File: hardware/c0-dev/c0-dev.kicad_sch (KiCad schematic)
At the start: 1 part, among them J3 Conn_01x05

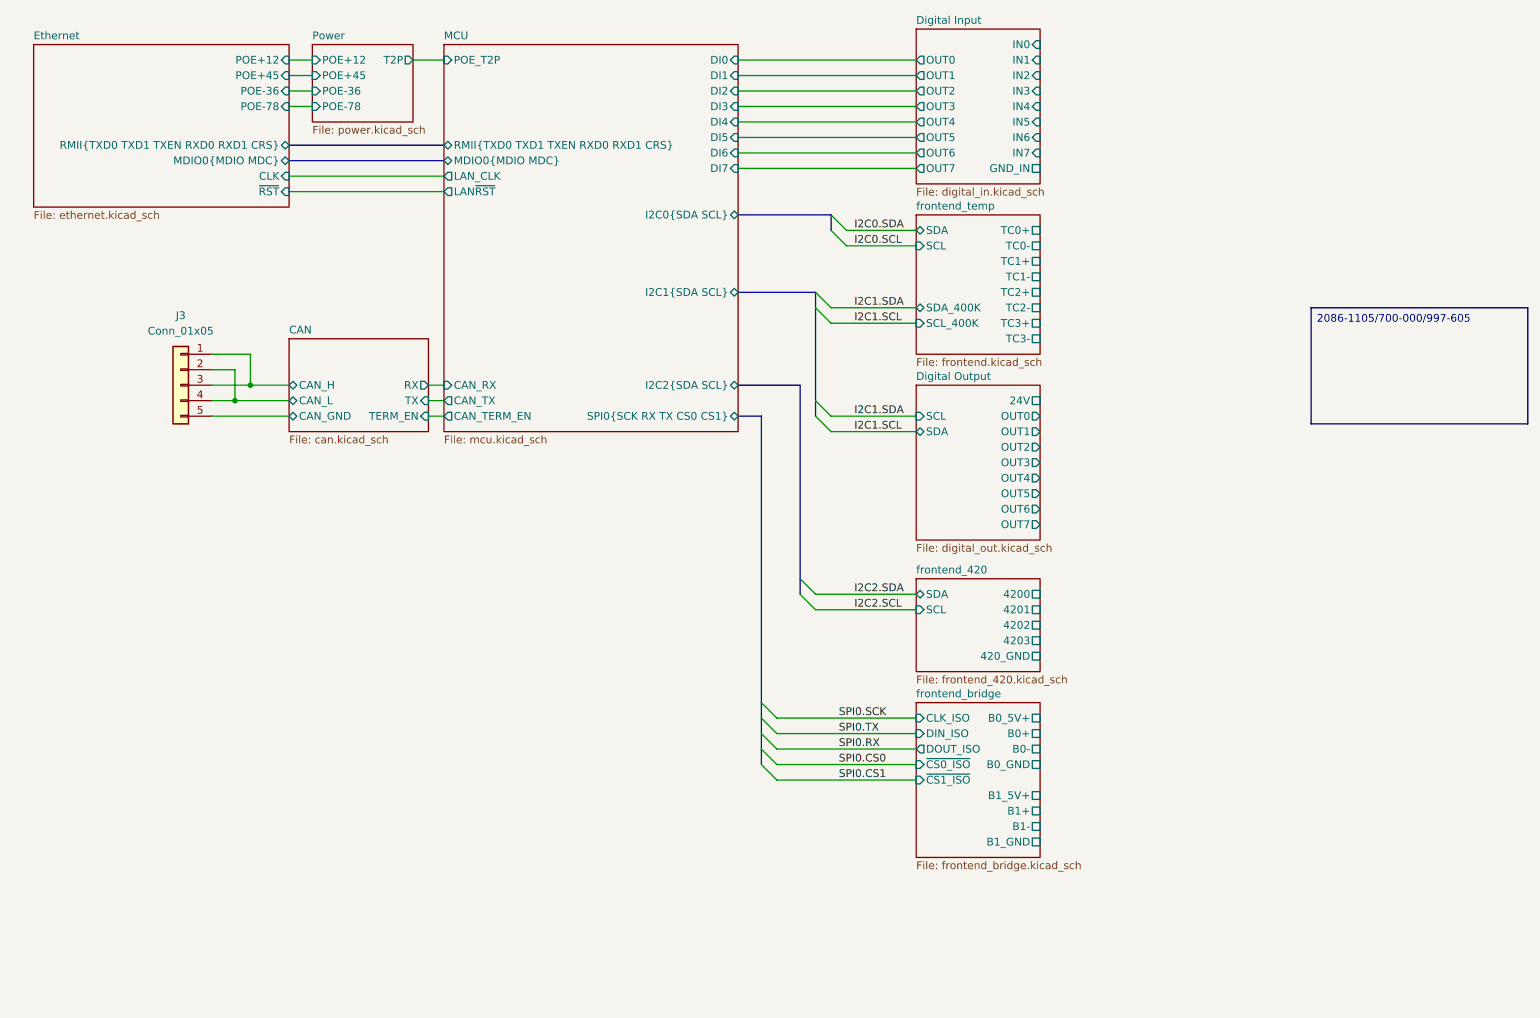
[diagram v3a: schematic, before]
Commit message: added connectors
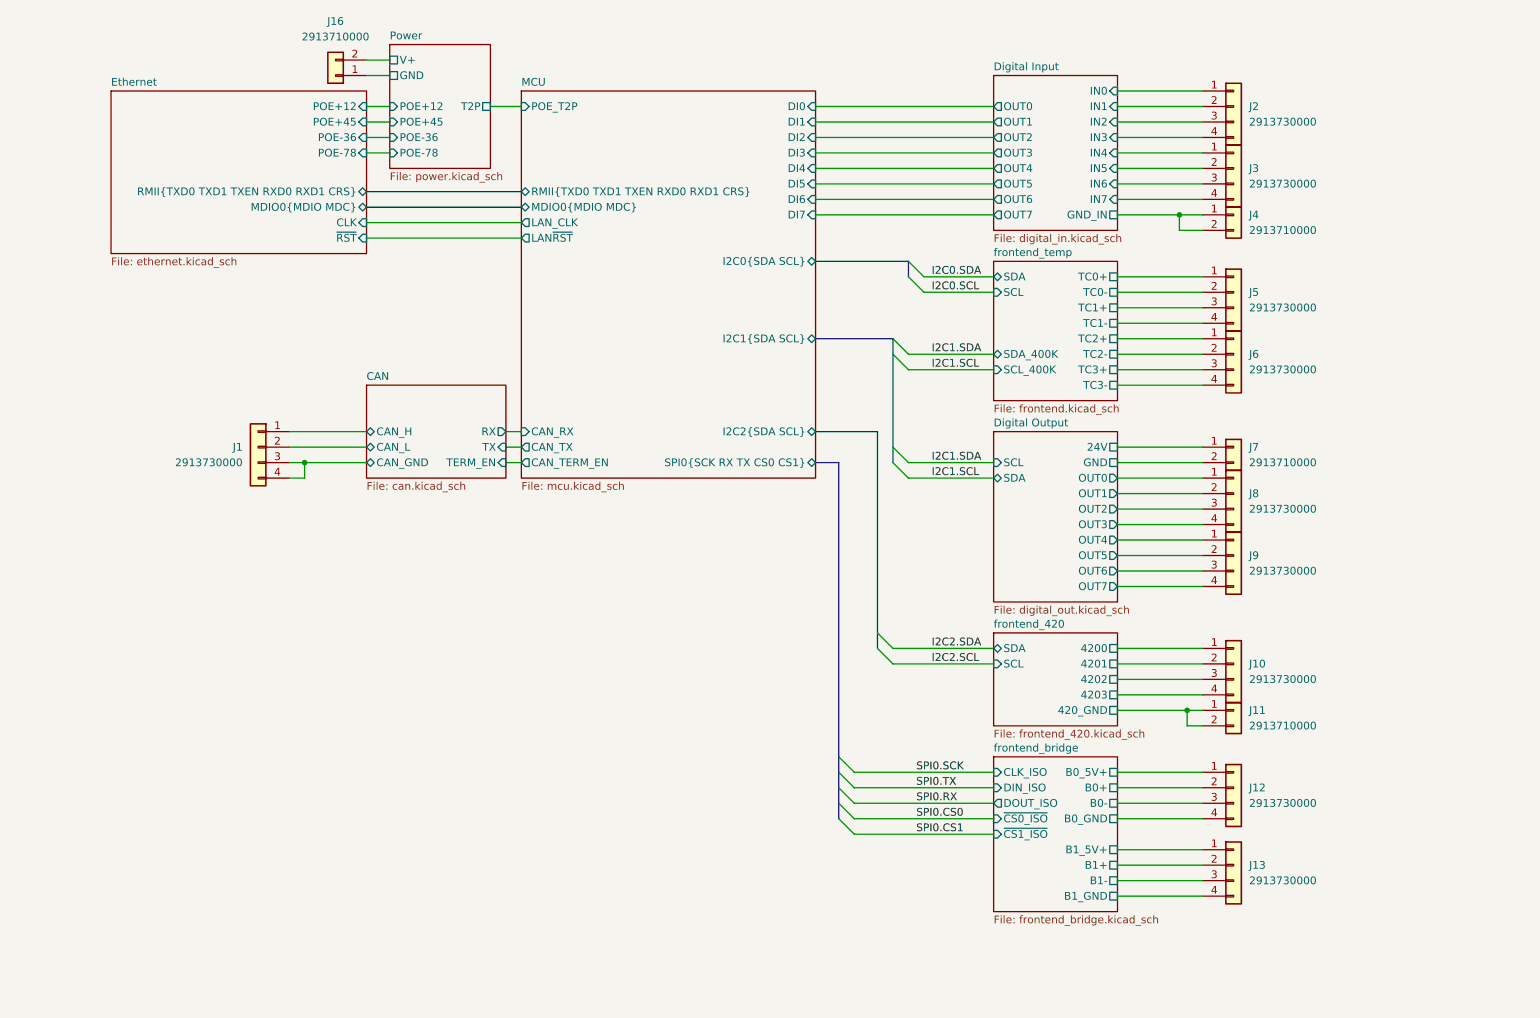
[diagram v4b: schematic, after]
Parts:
- removed J3: Conn_01x05, symbol Connector_Generic:Conn_01x05
- added J1, J10, J12, J13, J2, J3, J5, J6, J8, J9: 2913730000, symbol Connector_Generic:Conn_01x04
- added J11, J16, J4, J7: 2913710000, symbol Connector_Generic:Conn_01x02
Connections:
- net CAN/CAN_GND: now also J1.3 (Pin_3), J1.4 (Pin_4)
- net CAN/CAN_H: now also J1.1 (Pin_1)
- net CAN/CAN_L: now also J1.2 (Pin_2)
- net Digital Input/GND_IN: now also J4.1 (Pin_1), J4.2 (Pin_2)
- net Digital Input/IN0: now also J2.1 (Pin_1)
- net Digital Input/IN1: now also J2.2 (Pin_2)
- net Digital Input/IN2: now also J2.3 (Pin_3)
- net Digital Input/IN3: now also J2.4 (Pin_4)
- net Digital Input/IN4: now also J3.1 (Pin_1)
- net Digital Input/IN5: now also J3.2 (Pin_2)
- net Digital Input/IN6: now also J3.3 (Pin_3)
- net Digital Input/IN7: now also J3.4 (Pin_4)
- net Digital Output/24V: now also J7.1 (Pin_1)
- net Digital Output/OUT0: now also J8.1 (Pin_1)
- net Digital Output/OUT1: now also J8.2 (Pin_2)
- net Digital Output/OUT2: now also J8.3 (Pin_3)
- net Digital Output/OUT3: now also J8.4 (Pin_4)
- net Digital Output/OUT4: now also J9.1 (Pin_1)
- net Digital Output/OUT5: now also J9.2 (Pin_2)
- net Digital Output/OUT6: now also J9.3 (Pin_3)
- net Digital Output/OUT7: now also J9.4 (Pin_4)
- net frontend_420/4200: now also J10.1 (Pin_1)
- net frontend_420/4201: now also J10.2 (Pin_2)
- net frontend_420/4202: now also J10.3 (Pin_3)
- net frontend_420/4203: now also J10.4 (Pin_4)
- net frontend_420/420_GND: now also J11.1 (Pin_1), J11.2 (Pin_2)
- net frontend_bridge/B0+: now also J12.2 (Pin_2)
- net frontend_bridge/B0-: now also J12.3 (Pin_3)
- net frontend_bridge/B0_5V+: now also J12.1 (Pin_1)
- net frontend_bridge/B0_GND: now also J12.4 (Pin_4)
- net frontend_bridge/B1+: now also J13.2 (Pin_2)
- net frontend_bridge/B1-: now also J13.3 (Pin_3)
- net frontend_bridge/B1_5V+: now also J13.1 (Pin_1)
- net frontend_bridge/B1_GND: now also J13.4 (Pin_4)
- net frontend_temp/TC0+: now also J5.1 (Pin_1)
- net frontend_temp/TC0-: now also J5.2 (Pin_2)
- net frontend_temp/TC1+: now also J5.3 (Pin_3)
- net frontend_temp/TC1-: now also J5.4 (Pin_4)
- net frontend_temp/TC2+: now also J6.1 (Pin_1)
- net frontend_temp/TC2-: now also J6.2 (Pin_2)
- net frontend_temp/TC3+: now also J6.3 (Pin_3)
- net frontend_temp/TC3-: now also J6.4 (Pin_4)
- new net Digital Output/GND: J7.2 (Pin_2)
- new net Power/GND: J16.1 (Pin_1)
- new net Power/V+: J16.2 (Pin_2)
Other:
- sheet Digital Output ports: added GND; removed none
- sheet Power ports: added GND, V+; removed none

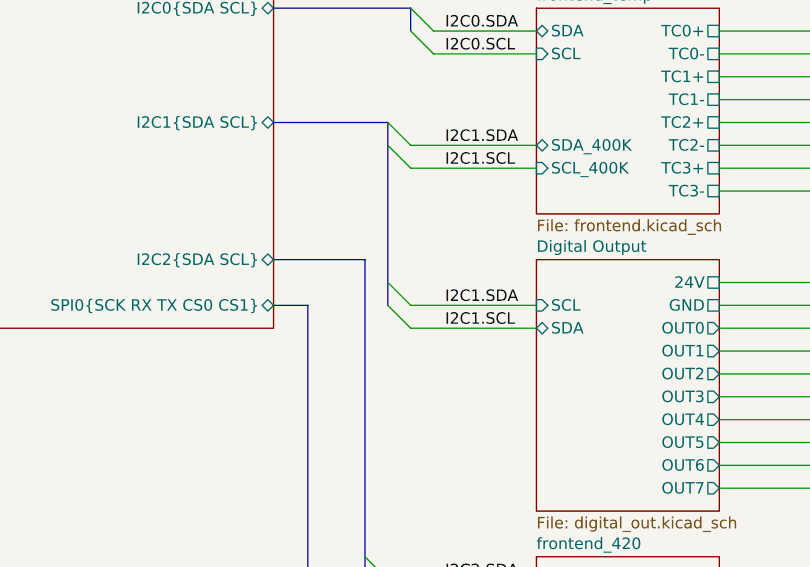
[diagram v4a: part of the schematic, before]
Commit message: added watchdog output disable
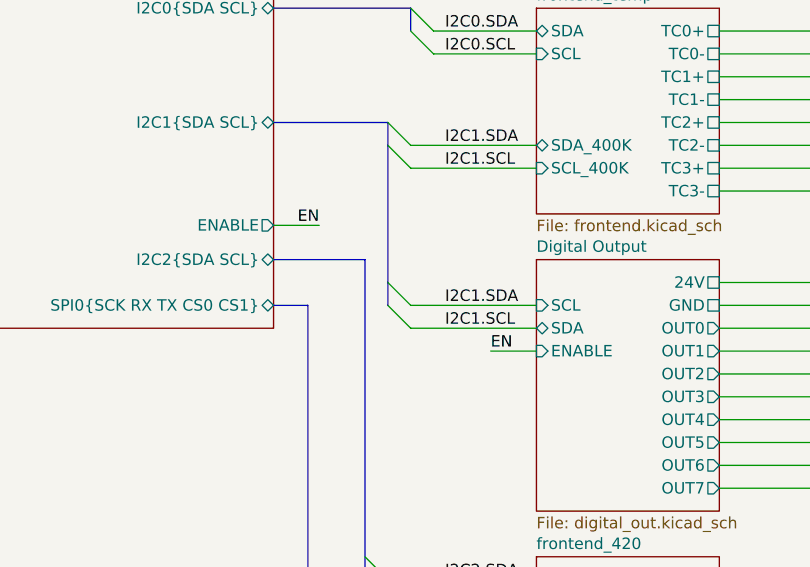
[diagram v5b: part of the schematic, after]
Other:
- sheet Digital Output ports: added ENABLE; removed none
- sheet MCU ports: added ENABLE; removed none
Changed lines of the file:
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@@
+	(wire
+		(pts
+			(xy 148.59 80.01) (xy 153.67 80.01)
+		)
+		(stroke
+			(width 0)
+			(type default)
+		)
+	)
 	(wire
 		(pts
@@
 		(pts
 			(xy 163.83 73.66) (xy 177.8 73.66)
+		)
+		(stroke
+			(width 0)
+			(type default)
+		)
+	)
+	(wire
+		(pts
+			(xy 172.72 93.98) (xy 177.8 93.98)
 		)
 		(stroke
@@
 		)
 	)
+	(label "EN"
+		(at 172.72 93.98 0)
+		(effects
+			(font
+				(size 1.27 1.27)
+			)
+			(justify left bottom)
+		)
+	)
 	(label "I2C0.SCL"
 		(at 167.64 60.96 0)
@@
 			)
 			(justify left bottom)
+		)
+	)
+	(label "EN"
+		(at 153.67 80.01 180)
+		(effects
+			(font
+				(size 1.27 1.27)
+			)
+			(justify right bottom)
 		)
 	)
@@
 			)
 		)
+		(pin "ENABLE" input
+			(at 177.8 93.98 180)
+			(effects
+				(font
+					(size 1.27 1.27)
+				)
+				(justify left)
+			)
+		)
 		(instances
 			(project "c0-dev"
@@
 			(effects
 				(font
+					(size 1.27 1.27)
+				)
+				(justify right)
+			)
+		)
+		(pin "ENABLE" output
+			(at 148.59 80.01 0)
+			(effects
+				(font

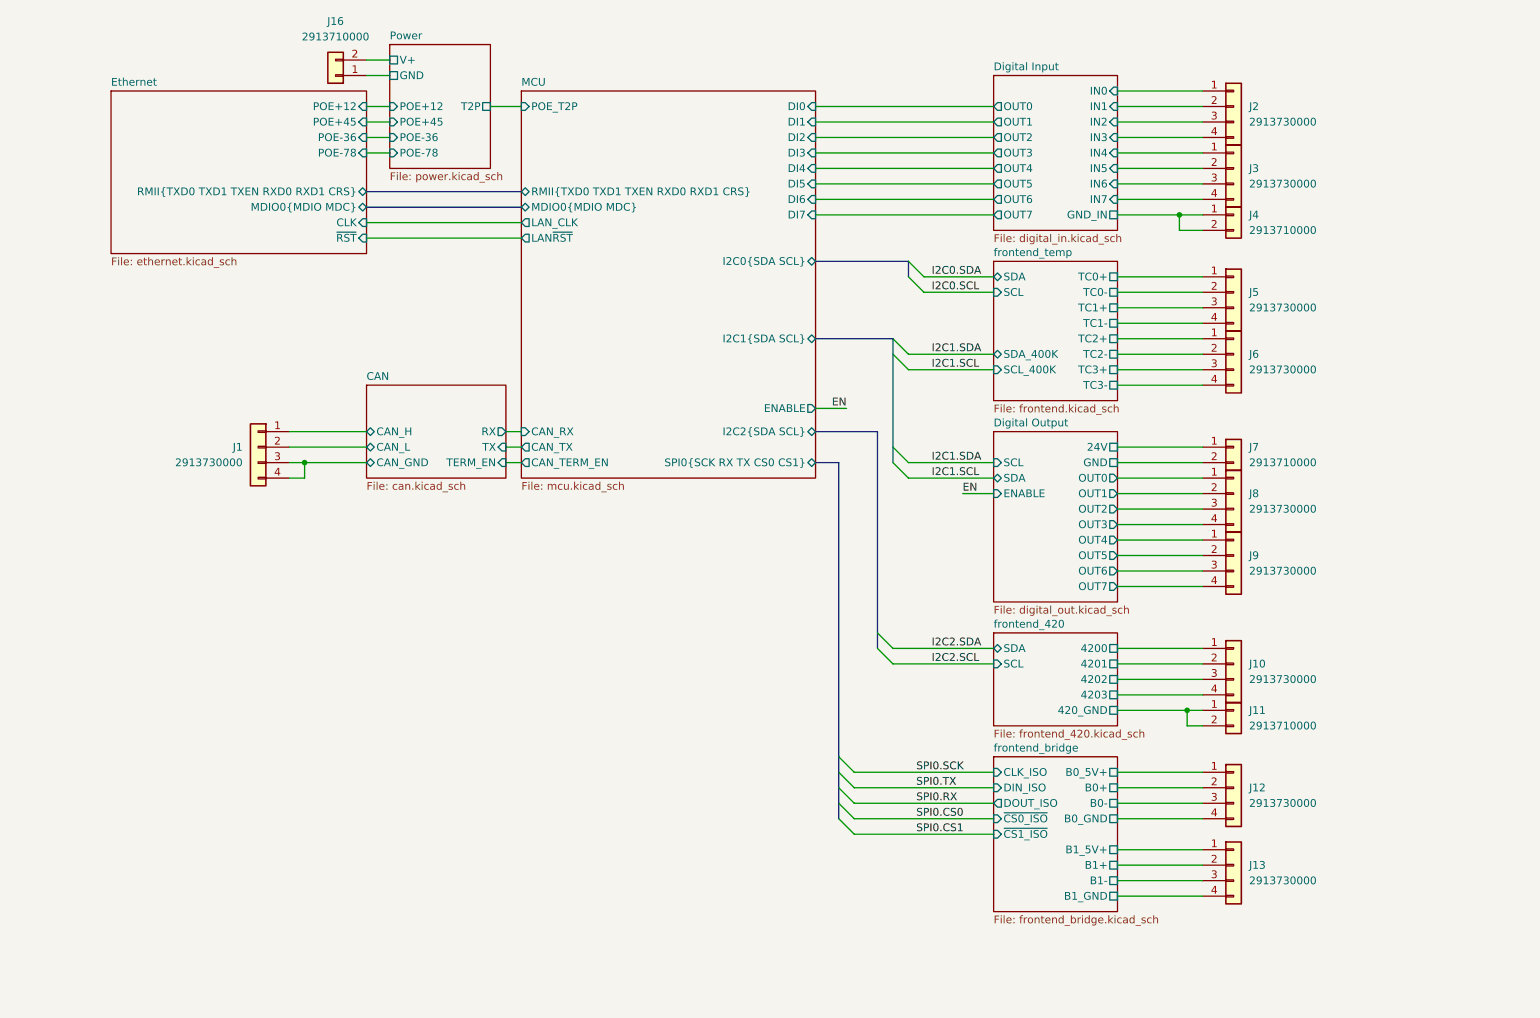
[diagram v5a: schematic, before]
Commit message: added 4-pin connector
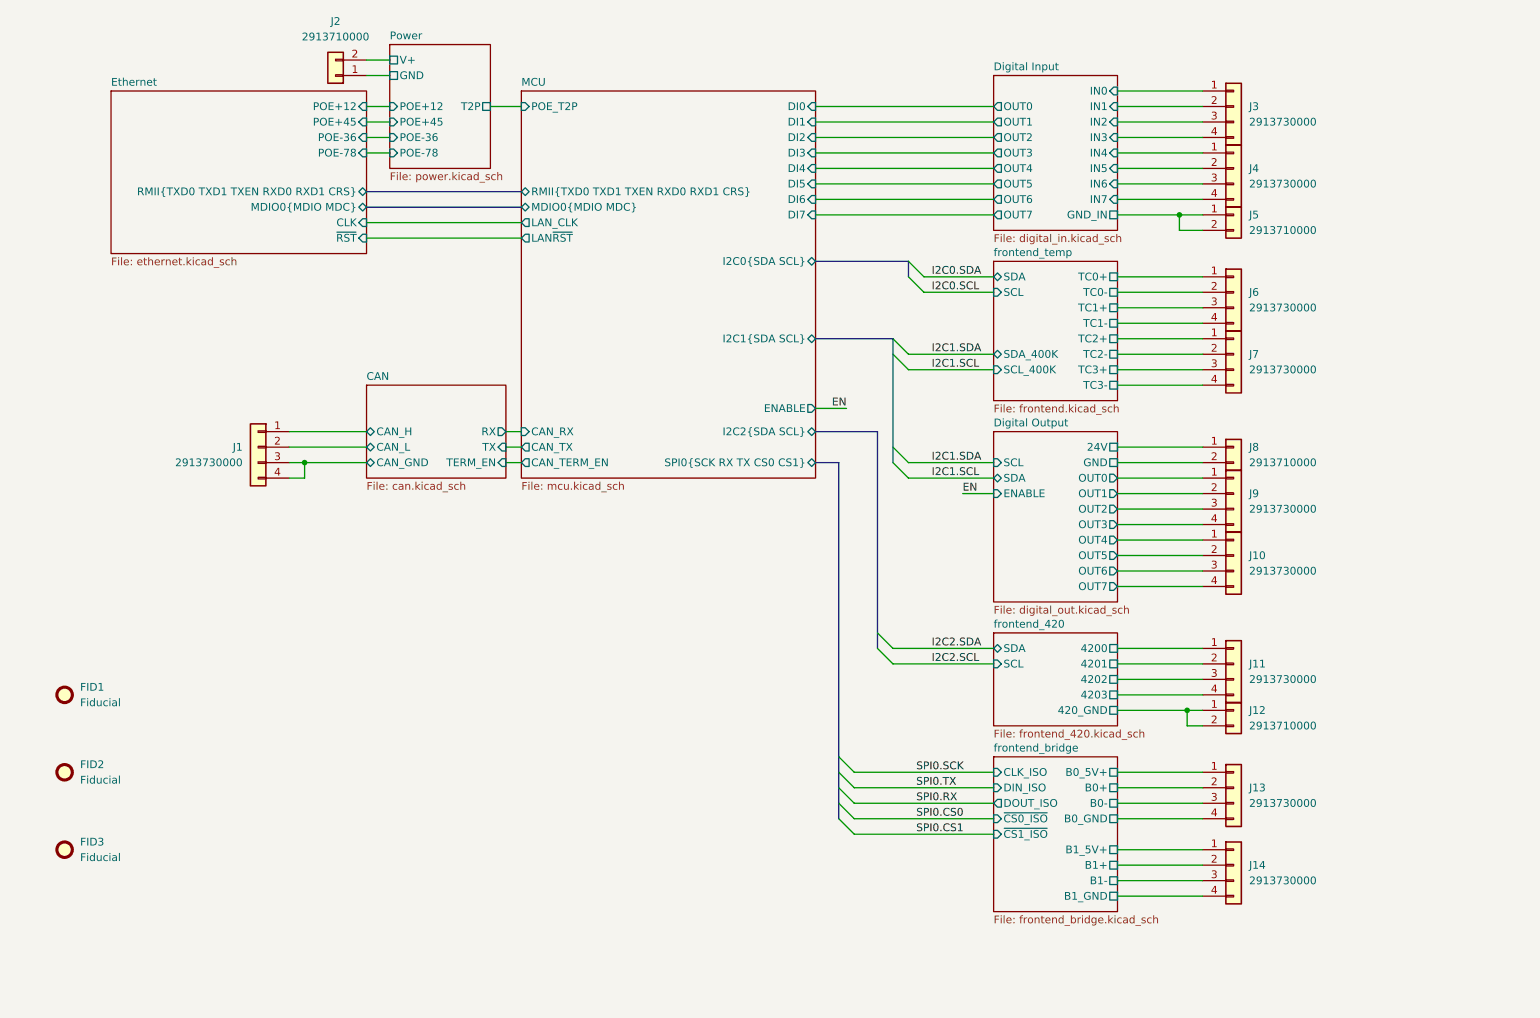
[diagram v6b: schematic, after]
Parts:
- removed J12, J3, J5, J8: 2913730000, symbol Connector_Generic:Conn_01x04
- added FID1, FID2, FID3: Fiducial, Fiducial:Fiducial_1mm_Mask2mm, symbol Mechanical:Fiducial
- added J11, J14, J4, J7: 2913730000, conduit:2913730000, symbol Connector_Generic:Conn_01x04
- J1, J10, J13, J6, J9: footprint (none) -> conduit:2913730000
- J3: renamed from J2; footprint (none) -> conduit:2913730000
- renumbered J11 to J12, J16 to J2, J4 to J5, J7 to J8
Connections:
- net Digital Input/IN4: now also J4.1 (Pin_1)
- net Digital Input/IN5: now also J4.2 (Pin_2)
- net Digital Input/IN6: now also J4.3 (Pin_3)
- net Digital Input/IN7: now also J4.4 (Pin_4)
- net Digital Output/OUT0: now also J9.1 (Pin_1)
- net Digital Output/OUT1: now also J9.2 (Pin_2)
- net Digital Output/OUT2: now also J9.3 (Pin_3)
- net Digital Output/OUT3: now also J9.4 (Pin_4)
- net Digital Output/OUT4: now also J10.1 (Pin_1); no longer J9.1 (Pin_1)
- net Digital Output/OUT5: now also J10.2 (Pin_2); no longer J9.2 (Pin_2)
- net Digital Output/OUT6: now also J10.3 (Pin_3); no longer J9.3 (Pin_3)
- net Digital Output/OUT7: now also J10.4 (Pin_4); no longer J9.4 (Pin_4)
- net frontend_420/4200: now also J11.1 (Pin_1); no longer J10.1 (Pin_1)
- net frontend_420/4201: now also J11.2 (Pin_2); no longer J10.2 (Pin_2)
- net frontend_420/4202: now also J11.3 (Pin_3); no longer J10.3 (Pin_3)
- net frontend_420/4203: now also J11.4 (Pin_4); no longer J10.4 (Pin_4)
- net frontend_bridge/B0+: now also J13.2 (Pin_2)
- net frontend_bridge/B0-: now also J13.3 (Pin_3)
- net frontend_bridge/B0_5V+: now also J13.1 (Pin_1)
- net frontend_bridge/B0_GND: now also J13.4 (Pin_4)
- net frontend_bridge/B1+: now also J14.2 (Pin_2); no longer J13.2 (Pin_2)
- net frontend_bridge/B1-: now also J14.3 (Pin_3); no longer J13.3 (Pin_3)
- net frontend_bridge/B1_5V+: now also J14.1 (Pin_1); no longer J13.1 (Pin_1)
- net frontend_bridge/B1_GND: now also J14.4 (Pin_4); no longer J13.4 (Pin_4)
- net frontend_temp/TC0+: now also J6.1 (Pin_1)
- net frontend_temp/TC0-: now also J6.2 (Pin_2)
- net frontend_temp/TC1+: now also J6.3 (Pin_3)
- net frontend_temp/TC1-: now also J6.4 (Pin_4)
- net frontend_temp/TC2+: now also J7.1 (Pin_1); no longer J6.1 (Pin_1)
- net frontend_temp/TC2-: now also J7.2 (Pin_2); no longer J6.2 (Pin_2)
- net frontend_temp/TC3+: now also J7.3 (Pin_3); no longer J6.3 (Pin_3)
- net frontend_temp/TC3-: now also J7.4 (Pin_4); no longer J6.4 (Pin_4)
